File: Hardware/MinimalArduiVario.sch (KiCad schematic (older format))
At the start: 35 parts, among them IC1 ATMEGA328P-A, SW1 Select, SW2 Up, SW3 Down

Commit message: dev proto hardware v1
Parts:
- removed J?: CONN_02X04, symbol CONN_02X04
- added J2: CONN_01X08, Pin_Headers:Pin_Header_Angled_1x08_Pitch2.54mm, symbol CONN_01X08
- R7, R8: renamed from R?; value 1K -> 4K7
- R9: renamed from R?; value R -> 500
- SW1, SW2, SW3: footprint Buttons_Switches_ThroughHole:SW_Tactile_SPST_Angled -> Buttons_Switches_THT:SW_Tactile_SPST_Angled
- SW4: renamed from SW?; footprint Buttons_Switches_ThroughHole:SW_Tactile_SPST_Angled -> Buttons_Switches_THT:SW_Tactile_SPST_Angled
- gave numbers to parts that had none: 21
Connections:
- net BTN1: now also IC1.26 ((PCINT11/ADC3)PC3); no longer IC1.32 ((PCINT18/INT0)PD2)
- net BTN2: now also IC1.24 ((PCINT9/ADC1)PC1); no longer IC1.1 ((PCINT19/OC2B/INT1)PD3)
- net BTN3: now also IC1.25 ((PCINT10/ADC2)PC2); no longer IC1.2 ((PCINT20/XCK/T0)PD4)
- net GND: now also J2.2 (P2)
- net MISO: now also J2.4 (P4)
- net MOSI: now also J2.5 (P5)
- net RST: now also J2.8 (P8)
- net Rx: now also J2.7 (P7)
- net SCK-RED: now also J2.3 (P3)
- net Tx: now also J2.6 (P6)
- net at R6.2: now also J2.1 (P1)
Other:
- note added: "id = 20mA"
- moved on the sheet: D2, R6

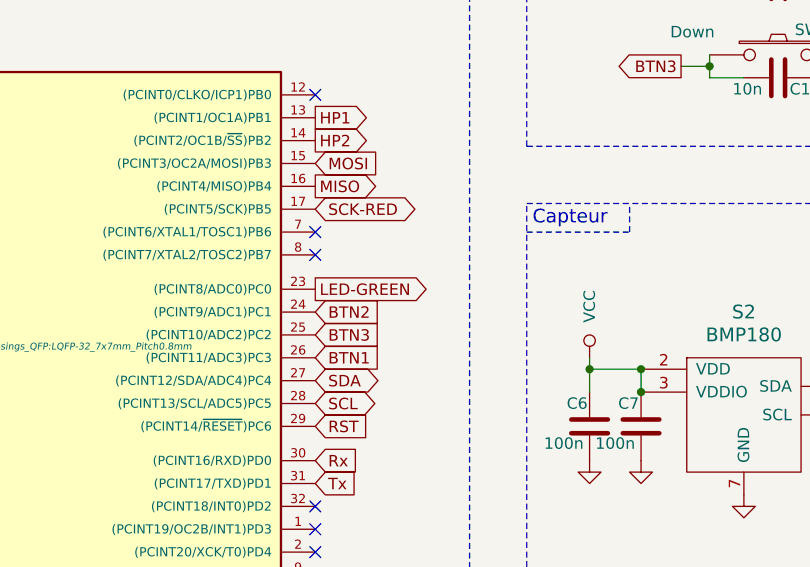
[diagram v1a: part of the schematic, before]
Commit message: Prepare dev software
Change Adafruit lib for BMP180 and test all peripherals. Set fuses into "extra_script.py".
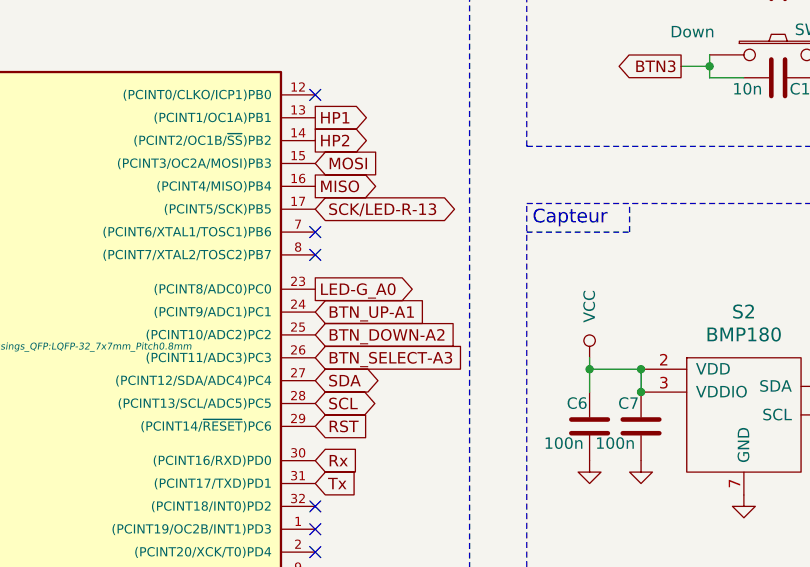
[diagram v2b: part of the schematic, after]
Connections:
- net BTN1: no longer IC1.26 ((PCINT11/ADC3)PC3)
- net BTN2: no longer IC1.24 ((PCINT9/ADC1)PC1)
- net BTN3: no longer IC1.25 ((PCINT10/ADC2)PC2)
- net LED-GREEN: no longer IC1.23 ((PCINT8/ADC0)PC0)
- net SCK-RED: no longer IC1.17 ((PCINT5/SCK)PB5)
- new net BTN_DOWN-A2: IC1.25 ((PCINT10/ADC2)PC2)
- new net BTN_SELECT-A3: IC1.26 ((PCINT11/ADC3)PC3)
- new net BTN_UP-A1: IC1.24 ((PCINT9/ADC1)PC1)
- new net LED-G_A0: IC1.23 ((PCINT8/ADC0)PC0)
- new net SCK/LED-R-13: IC1.17 ((PCINT5/SCK)PB5)
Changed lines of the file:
@@
 $EndComp
 Text GLabel 3100 5000 2    50   Input ~ 0
-BTN1
+BTN_SELECT-A3
 Text GLabel 3100 4800 2    50   Input ~ 0
-BTN2
+BTN_UP-A1
 Text GLabel 4700 2875 0    50   Output ~ 0
 BTN1
@@
 Press ON - Hold OFF \nLatching circuit\n
 Text GLabel 3100 4700 2    50   Output ~ 0
-LED-GREEN
+LED-G_A0
 Text GLabel 3100 4350 2    50   BiDi ~ 0
-SCK-RED
+SCK/LED-R-13
 $Comp
 L C C7
@@
 $EndComp
 Text GLabel 3100 4900 2    50   Input ~ 0
-BTN3
+BTN_DOWN-A2
 $EndSCHEMATC

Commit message: remove pin arduino
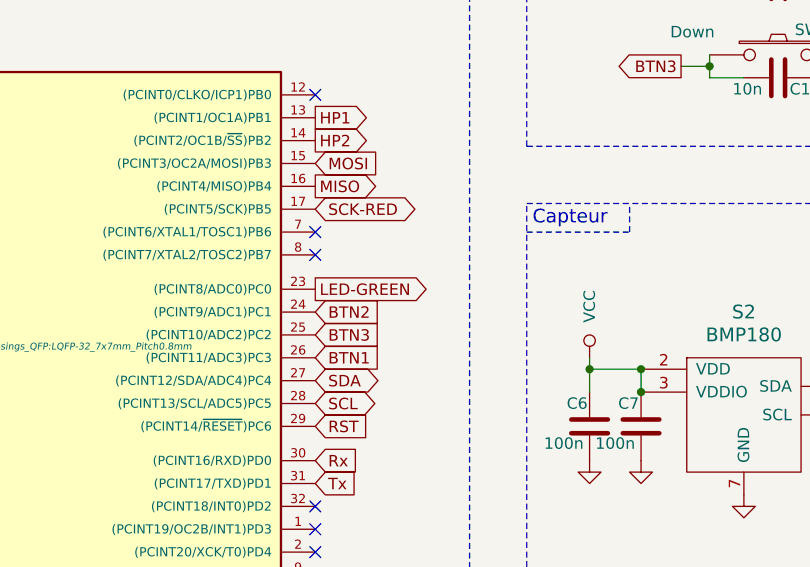
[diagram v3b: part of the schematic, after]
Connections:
- net BTN_DOWN-A2 is gone; now on net BTN3: IC1.25 ((PCINT10/ADC2)PC2)
- net BTN_SELECT-A3 is gone; now on net BTN1: IC1.26 ((PCINT11/ADC3)PC3)
- net BTN_UP-A1 is gone; now on net BTN2: IC1.24 ((PCINT9/ADC1)PC1)
- net LED-G_A0 is gone; now on net LED-GREEN: IC1.23 ((PCINT8/ADC0)PC0)
- net SCK/LED-R-13 is gone; now on net SCK-RED: IC1.17 ((PCINT5/SCK)PB5)
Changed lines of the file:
@@
 	1    0    0    -1
 $EndComp
-Text GLabel 3100 5000 2    50   Input ~ 0
-BTN_SELECT-A3
-Text GLabel 3100 4800 2    50   Input ~ 0
-BTN_UP-A1
 Text GLabel 4700 2875 0    50   Output ~ 0
 BTN1
@@
 Text Notes 650  1875 0    60   ~ 0
 Press ON - Hold OFF \nLatching circuit\n
-Text GLabel 3100 4700 2    50   Output ~ 0
-LED-G_A0
-Text GLabel 3100 4350 2    50   BiDi ~ 0
-SCK/LED-R-13
 $Comp
 L C C7
@@
 	-1   0    0    1
 $EndComp
+Text GLabel 3100 4350 2    50   BiDi ~ 0
+SCK-RED
+Text GLabel 3100 4700 2    50   Output ~ 0
+LED-GREEN
 Text GLabel 3100 4900 2    50   Input ~ 0
-BTN_DOWN-A2
+BTN3
+Text GLabel 3100 5000 2    50   Input ~ 0
+BTN1
+Text GLabel 3100 4800 2    50   Input ~ 0
+BTN2
 $EndSCHEMATC

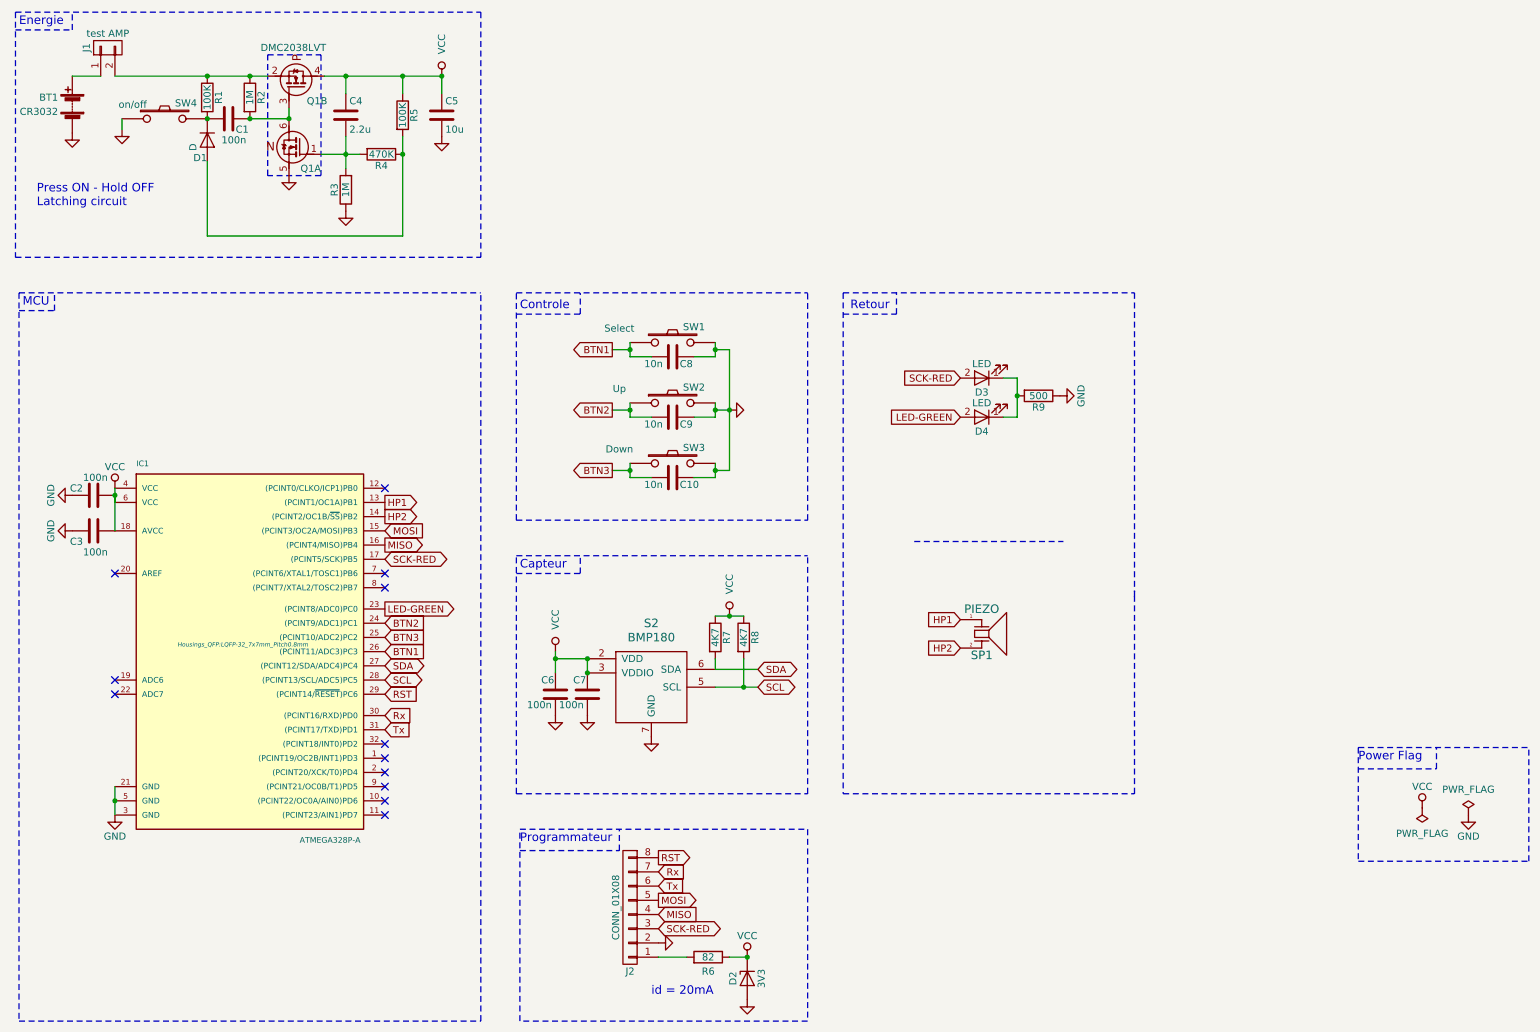
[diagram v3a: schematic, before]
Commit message: add somes function to manage power
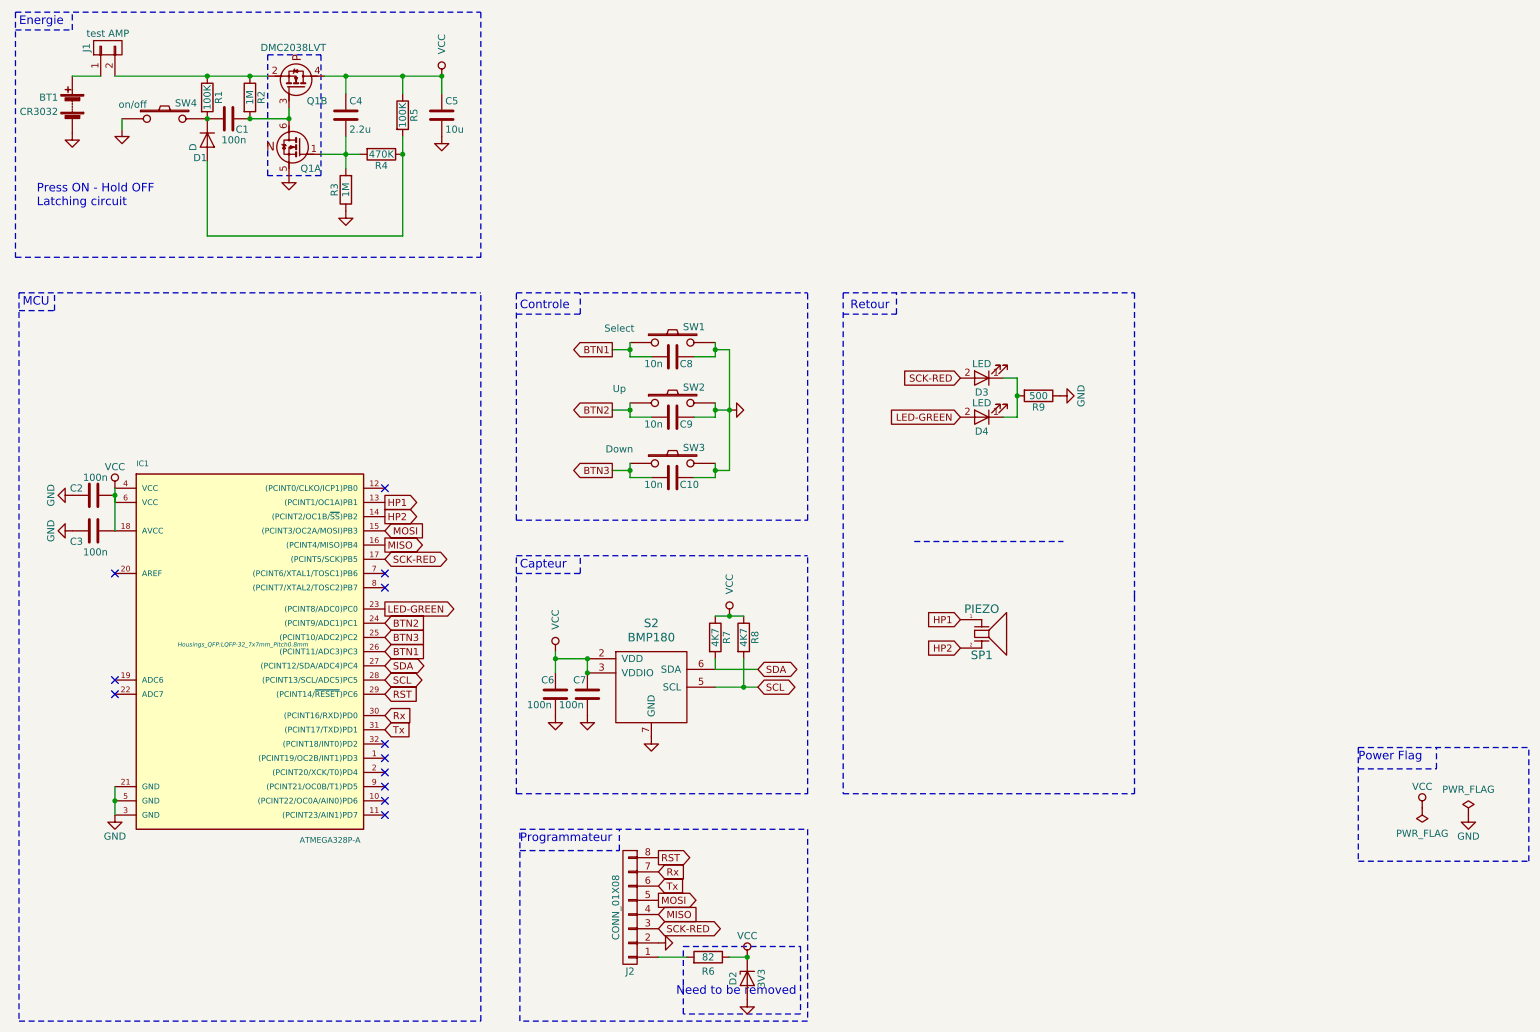
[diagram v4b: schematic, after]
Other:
- note added: "Need to be removed"
- note removed: "id = 20mA"
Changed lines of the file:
@@
 $EndComp
 Wire Wire Line
-	1200 5950 1200 6050
-Wire Wire Line
-	1200 6050 1200 6150
+	1200 5950 1200 6150
 Connection ~ 1200 6050
 Wire Wire Line
 	5425 2925 5275 2925
 Wire Wire Line
-	5425 2825 5425 2875
-Wire Wire Line
-	5425 2875 5425 2925
+	5425 2825 5425 2925
 Wire Wire Line
 	4825 2925 4975 2925
 Wire Wire Line
-	4825 2825 4825 2875
-Wire Wire Line
-	4825 2875 4825 2925
-Wire Wire Line
-	4825 3250 4825 3300
-Wire Wire Line
-	4825 3300 4825 3350
+	4825 2825 4825 2925
+Wire Wire Line
+	4825 3250 4825 3350
 Wire Wire Line
 	4825 3350 4975 3350
@@
 	5425 3350 5275 3350
 Wire Wire Line
-	5425 3250 5425 3300
-Wire Wire Line
-	5425 3300 5425 3350
-Wire Wire Line
-	4825 3675 4825 3725
-Wire Wire Line
-	4825 3725 4825 3775
+	5425 3250 5425 3350
+Wire Wire Line
+	4825 3675 4825 3775
 Wire Wire Line
 	4825 3775 4975 3775
@@
 	5425 3775 5275 3775
 Wire Wire Line
-	5425 3675 5425 3725
-Wire Wire Line
-	5425 3725 5425 3775
+	5425 3675 5425 3775
 Wire Wire Line
 	5425 2875 5525 2875
@@
 Connection ~ 4825 3725
 Wire Wire Line
-	5525 2875 5525 3300
-Wire Wire Line
-	5525 3300 5525 3725
+	5525 2875 5525 3725
 Connection ~ 4825 3300
 Wire Wire Line
@@
 	4825 3725 4700 3725
 Wire Wire Line
-	1200 3850 1200 3900
-Wire Wire Line
-	1200 3900 1200 4150
+	1200 3850 1200 4150
 Connection ~ 1200 3900
 Wire Wire Line
@@
 	5425 5125 5425 5050
 Wire Wire Line
-	5425 5250 5625 5250
-Wire Wire Line
-	5625 5250 5725 5250
+	5425 5250 5725 5250
 Wire Wire Line
 	5625 5250 5625 5050
@@
 Connection ~ 4525 5050
 Wire Wire Line
-	5425 4750 5525 4750
-Wire Wire Line
-	5525 4750 5625 4750
+	5425 4750 5625 4750
 Connection ~ 5525 4750
 Connection ~ 4300 5050
 Wire Wire Line
-	4300 5000 4300 5050
-Wire Wire Line
-	4300 5050 4300 5150
+	4300 5000 4300 5150
 Wire Notes Line
 	6075 7600 4050 7600
@@
 	2425 1250 2150 1250
 Wire Wire Line
-	1200 950  1850 950
-Wire Wire Line
-	1850 950  2150 950
-Wire Wire Line
-	2150 950  2275 950
+	1200 950  2275 950
 Connection ~ 2150 950
 Wire Wire Line
@@
 Connection ~ 1850 950
 Wire Wire Line
-	2675 950  2825 950
-Wire Wire Line
-	2825 950  3225 950
-Wire Wire Line
-	3225 950  3500 950
+	2675 950  3500 950
 Wire Wire Line
 	3225 950  3225 1075
@@
 Connection ~ 2825 950
 Wire Wire Line
-	2650 1500 2825 1500
-Wire Wire Line
-	2825 1500 2925 1500
-Wire Wire Line
-	2825 1375 2825 1500
-Wire Wire Line
-	2825 1500 2825 1600
+	2650 1500 2925 1500
+Wire Wire Line
+	2825 1375 2825 1600
 Connection ~ 2825 1500
 Wire Wire Line
-	3225 1375 3225 1500
-Wire Wire Line
-	3225 1500 3225 2075
+	3225 1375 3225 2075
 Wire Wire Line
 	3225 2075 1850 2075
@@
 	7450 3075 7550 3075
 Wire Wire Line
-	7550 3075 7550 3200
-Wire Wire Line
-	7550 3200 7550 3350
+	7550 3075 7550 3350
 Wire Wire Line
 	7550 3350 7450 3350
@@
 Wire Wire Line
 	5225 7150 5025 7150
-Text Notes 4975 7425 0    60   ~ 0
-id = 20mA
+Text Notes 5150 7425 0    60   ~ 0
+Need to be removed
 $Comp
 L CONN_01X08 J2
@@
 Text GLabel 3100 4800 2    50   Input ~ 0
 BTN2
+Wire Notes Line
+	5200 7075 6025 7075
+Wire Notes Line
+	6025 7075 6025 7550
+Wire Notes Line
+	6025 7550 5200 7550
+Wire Notes Line
+	5200 7550 5200 7075
 $EndSCHEMATC
